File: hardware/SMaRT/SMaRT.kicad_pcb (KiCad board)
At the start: 4 copper layers, 40 x 105 mm, 29 parts, among them J1 Glider, J10 Conn_01x08, J11 Conn_01x08, J13 Power_TP, J2 Sensor, J3 TestPins_Sensor, J4 TestPins_Sensor, J5 Programmer, J6 Conn_01x03, J6 Conn_02x04_Odd_Even, J7 Conn_01x04, J8 Conn_01x04, J9 Conn_01x06, U1 MP1584, U2 MAX3232_SPARKFUN, U3 MAX3232_SPARKFUN

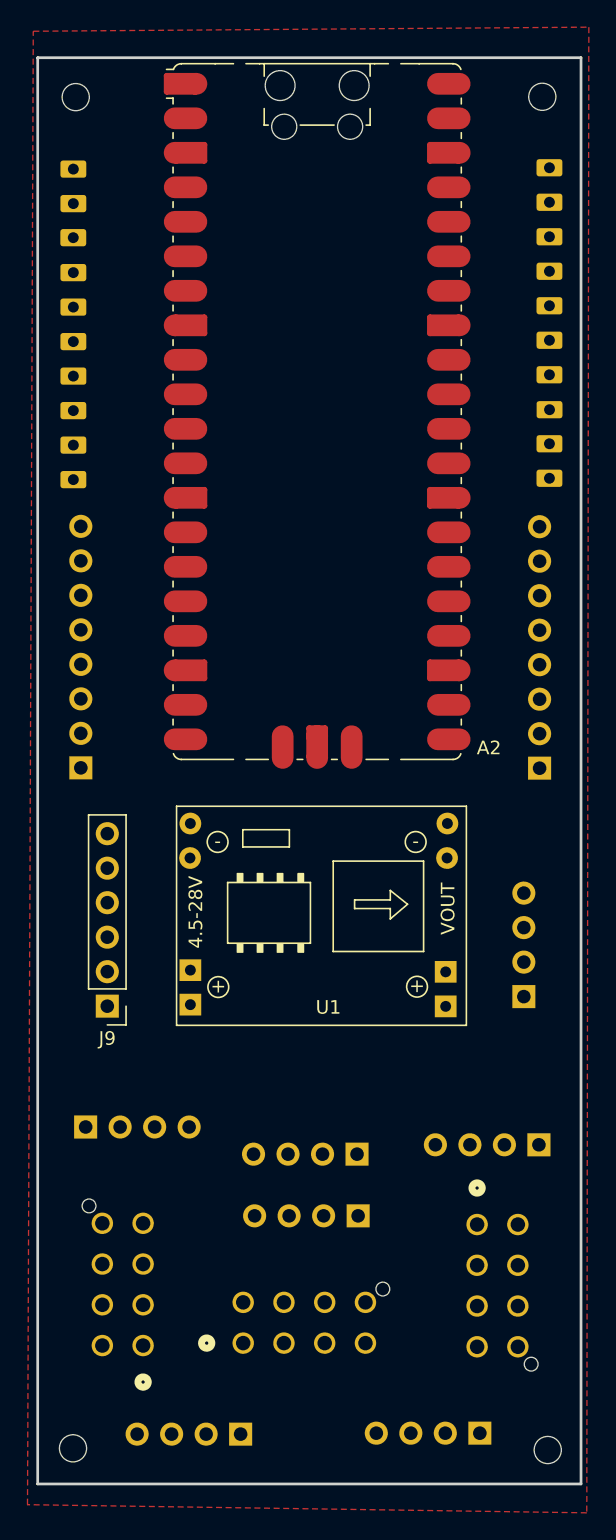
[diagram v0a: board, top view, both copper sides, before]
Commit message: added openlog, relay, switch
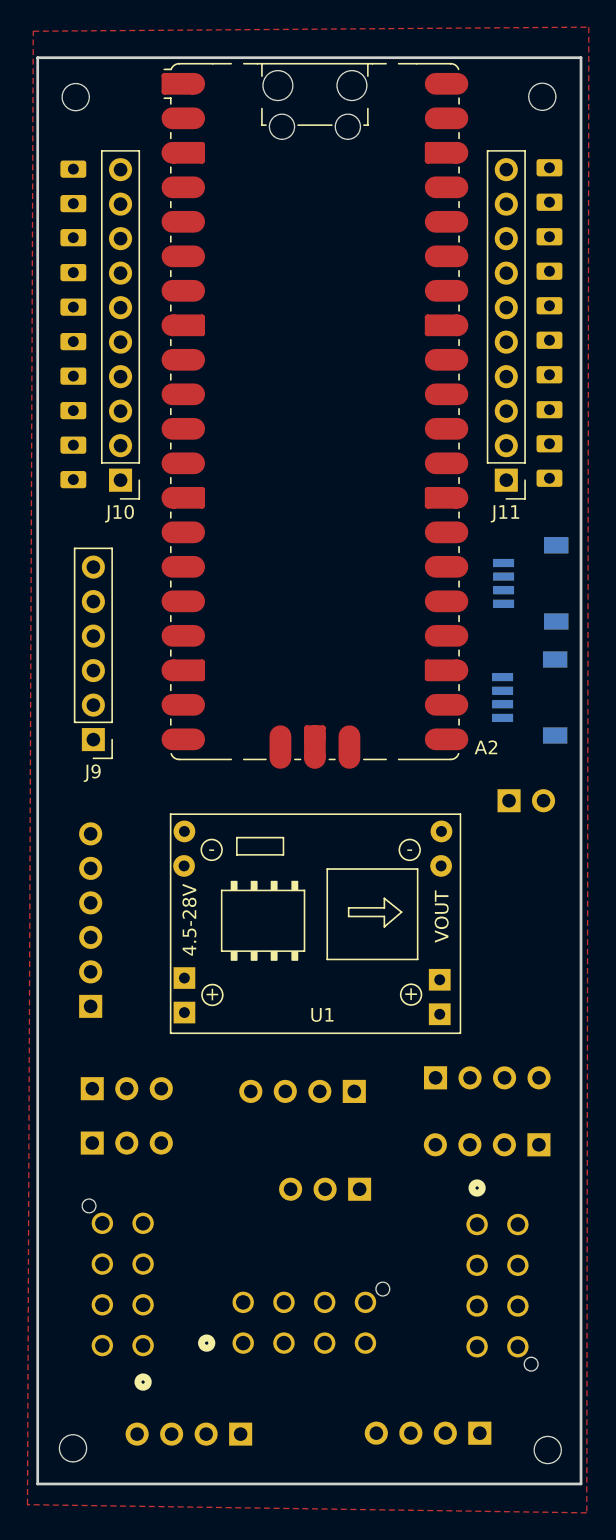
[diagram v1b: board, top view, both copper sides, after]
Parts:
- removed the J6 at (91.4, 117.1)
- added J12: Qwiic_Connector, Qwiic:Qwiic, B.Cu at (104.6, 75.1)
- added J13: Qwiic_Connector, Qwiic:Qwiic, B.Cu at (104.5, 83.5)
- added J14: SWITCH, Connector_PinHeader_2.54mm:PinHeader_1x02_P2.54mm_Vertical, B.Cu at (102.6, 91.1)
- added JP1: Jumper_3_Open, Connector_PinHeader_2.54mm:PinHeader_1x03_P2.54mm_Vertical, B.Cu at (71.9, 112.3)
- added JP2: Jumper_3_Open, Connector_PinHeader_2.54mm:PinHeader_1x03_P2.54mm_Vertical, B.Cu at (71.9, 116.3)
- added U4: OPENLOG, OpenLog:OpenLog, B.Cu at (70.4, 108.0)
- J10, J11: value Conn_01x08 -> Conn_01x10; footprint Connector_PinHeader_2.54mm:PinHeader_1x08_P2.54mm_Vertical -> Connector_PinHeader_2.54mm:PinHeader_1x10_P2.54mm_Vertical; moved to F.Cu
- J3: value TestPins_Sensor -> TestPins_Glider
- J6: footprint Connector_PinHeader_2.54mm:PinHeader_1x04_P2.54mm_Vertical -> Connector_PinHeader_2.54mm:PinHeader_1x03_P2.54mm_Vertical
- U1: footprint MPT1584:SRT_MPT1584EN_Module -> MPT1684:MPT1584EN_Module
- moved J13 26.0 mm to (97.2, 111.5)
- moved J10 21.4 mm to (74.0, 67.5), turned to 180 degrees
- moved J11 21.3 mm to (102.4, 67.5), turned to 180 degrees
- moved J9 19.7 mm to (72.0, 86.6)
- moved J4 14.3 mm to (91.2, 112.5), turned to 90 degrees
- moved J6 1.96 mm to (91.6, 119.7)
- moved U1 0.73 mm to (88.8, 99.6)
- moved A2 0.17 mm to (88.3, 62.5)
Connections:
- A2 pad 16: unconnected-(A2-GPIO12-Pad16) -> Net-(A2-GPIO12)
- A2 pad 17: unconnected-(A2-GPIO13-Pad17) -> Net-(A2-GPIO13)
- A2 pad 19: unconnected-(A2-GPIO14-Pad19) -> Net-(A2-GPIO14)
- A2 pad 20: unconnected-(A2-GPIO15-Pad20) -> Net-(A2-GPIO15)
- A2 pad 21: unconnected-(A2-GPIO16-Pad21) -> Net-(A2-GPIO16)
- A2 pad 22: unconnected-(A2-GPIO17-Pad22) -> Net-(A2-GPIO17)
- A2 pad 4: Net-(A2-GPIO2) -> /SDA1
- A2 pad 5: Net-(A2-GPIO3) -> /SCL1
- J1 pad 3: Net-(U2-T1OUT) -> /G_RX
- J10 pad 1: Net-(A2-GPIO11) -> Net-(A2-GPIO15)
- J10 pad 2: Net-(A2-GPIO10) -> Net-(A2-GPIO14)
- J10 pad 3: Net-(A2-GPIO9) -> Net-(A2-GPIO13)
- J10 pad 4: Net-(A2-GPIO8) -> Net-(A2-GPIO12)
- J10 pad 5: Net-(A2-GPIO7) -> Net-(A2-GPIO11)
- J10 pad 6: Net-(A2-GPIO6) -> Net-(A2-GPIO10)
- J10 pad 7: Net-(A2-GPIO3) -> Net-(A2-GPIO9)
- J10 pad 8: Net-(A2-GPIO2) -> Net-(A2-GPIO8)
- J11 pad 1: Net-(A2-GPIO18) -> Net-(A2-GPIO16)
- J11 pad 2: Net-(A2-GPIO19) -> Net-(A2-GPIO17)
- J11 pad 3: Net-(A2-GPIO20) -> Net-(A2-GPIO18)
- J11 pad 4: Net-(A2-GPIO21) -> Net-(A2-GPIO19)
- J11 pad 5: Net-(A2-ADC_VREF) -> Net-(A2-GPIO20)
- J11 pad 6: Net-(A2-GPIO26_ADC0) -> Net-(A2-GPIO21)
- J11 pad 7: Net-(A2-GPIO27_ADC1) -> Net-(A2-ADC_VREF)
- J11 pad 8: Net-(A2-AGND) -> Net-(A2-GPIO26_ADC0)
- J2 pad 3: /S_TX -> /S_RX
- J2 pad 4: /S_RX -> /S_TX
- J3 pad 3: VCC -> /G_RX
- U1 pad 1: VCC -> Net-(J14-Pin_1)
- U1 pad 2: VCC -> Net-(J14-Pin_1)
- U2 pad 1: Net-(U2-T1OUT) -> /G_RX
- U3 pad 10: /RX1 -> /S_RX_TTL
- U3 pad 8: /TX1 -> /S_TX_TTL
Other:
- board text added: "3V3"
- board text added: "5"
- board text added: "5V"
- board text added: "6"
- board text added: "7"
- board text added: "8"
- board text added: "OL"
- board text added: "RP"
- board text added: "SWITCH"

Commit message: relay addition
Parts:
- added JP3: Jumper_3_Open, Connector_PinHeader_2.54mm:PinHeader_1x03_P2.54mm_Vertical, B.Cu at (90.0, 117.5)
- added R1: R, Resistor_THT:R_Axial_DIN0207_L6.3mm_D2.5mm_P7.62mm_Horizontal, F.Cu at (75.0, 103.7)
- added U5: ~, G3VM-41AY1:G3VM-41AY1, F.Cu at (103.7, 100.9)
- J14: value SWITCH -> Conn_01x02
- moved J6 2.26 mm to (90.0, 121.3)
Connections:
- A2 pad 21: Net-(A2-GPIO16) -> /RELAY
- A2 pad 29: unconnected-(A2-GPIO22-Pad29) -> Net-(A2-GPIO22)
- J11 pad 1: Net-(A2-GPIO16) -> Net-(A2-GPIO17)
- J11 pad 2: Net-(A2-GPIO17) -> Net-(A2-GPIO18)
- J11 pad 3: Net-(A2-GPIO18) -> Net-(A2-GPIO19)
- J11 pad 4: Net-(A2-GPIO19) -> Net-(A2-GPIO20)
- J11 pad 5: Net-(A2-GPIO20) -> Net-(A2-GPIO21)
- J11 pad 6: Net-(A2-GPIO21) -> Net-(A2-GPIO22)
- J2 pad 1: GND -> Net-(JP3-C)
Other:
- board text added: "RLY"

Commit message: hardware: update SMaRT board and ignore KiCad artifacts
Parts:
- removed the J13 at (97.2, 111.5)
- removed REF** (x4): MountingHole_2mm, MountingHole:MountingHole_2mm
- J13: renamed from J2; footprint Library:CONN_2068320000-SD_08_MOL -> MolexLib:CONN_2068320000-SD_08_MOL
- J5: renamed from J1; footprint Library:CONN_2068320000-SD_08_MOL -> MolexLib:CONN_2068320000-SD_08_MOL
- J8: renamed from J5; footprint Library:CONN_2068320000-SD_08_MOL -> MolexLib:CONN_2068320000-SD_08_MOL
- renumbered A2 to A1, J3 to J1, J9 to J10, J4 to J12, J7 to J14, J13 to J2, J12 to J3, J14 to J4, J8 to J6, J10 to J7, J6 to J9, JP3 to JP1, JP1 to JP2, JP2 to JP3, U5 to U3, U3 to U4, U4 to U5
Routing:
- removed copper zone on F.Cu, net GND

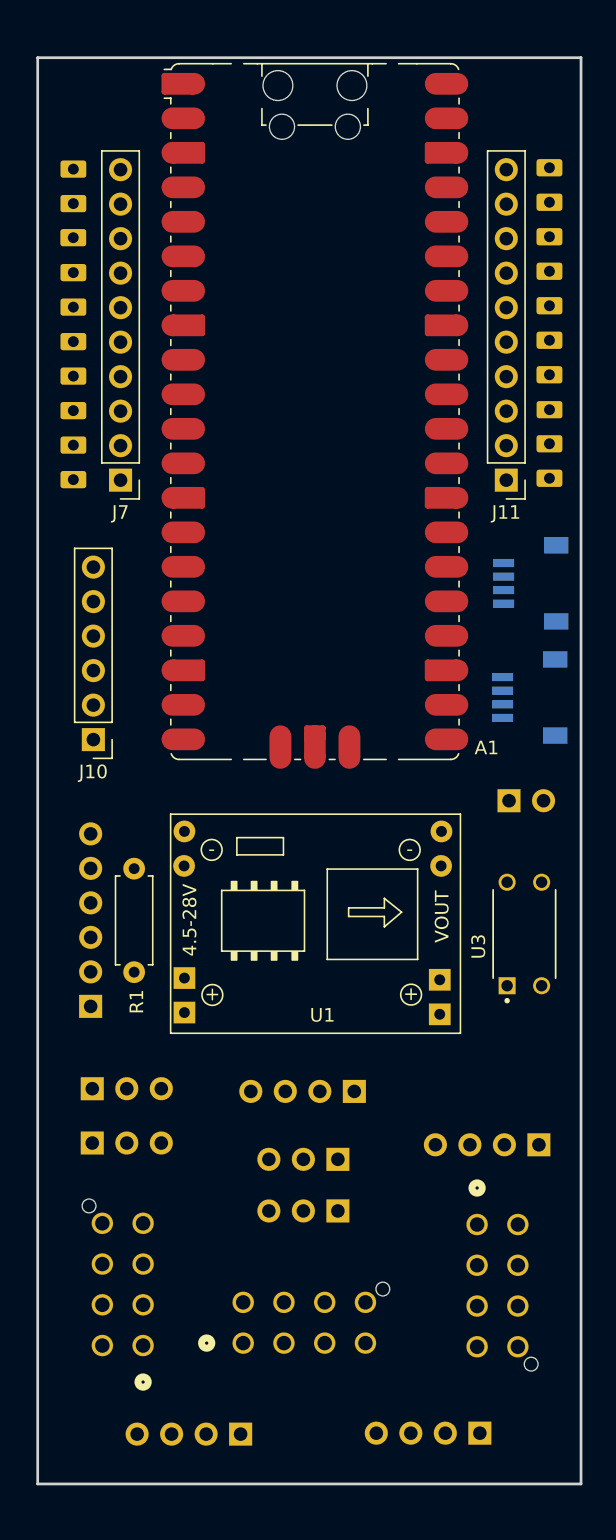
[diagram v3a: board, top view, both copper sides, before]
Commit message: hardware: add mounting holes and power test header
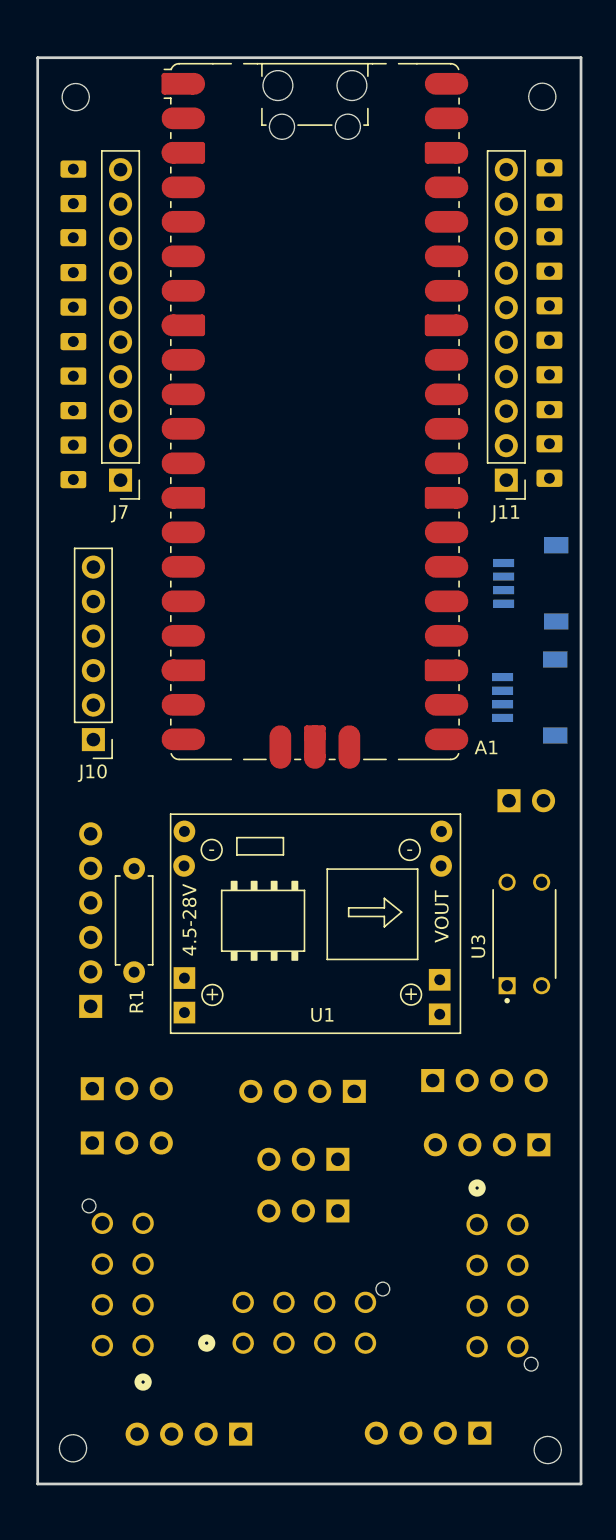
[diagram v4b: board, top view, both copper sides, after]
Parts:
- added J13: Power_TP, Connector_PinHeader_2.54mm:PinHeader_1x04_P2.54mm_Vertical, B.Cu at (97.0, 111.7)
- added REF**: MountingHole_2mm, MountingHole:MountingHole_2mm, F.Cu at (105.4, 138.9)
- added REF**: MountingHole_2mm, MountingHole:MountingHole_2mm, F.Cu at (70.7, 39.3)
- added REF**: MountingHole_2mm, MountingHole:MountingHole_2mm, F.Cu at (70.5, 138.8)
- added REF**: MountingHole_2mm, MountingHole:MountingHole_2mm, F.Cu at (105.0, 39.3)

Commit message: hardware: update PCB and schematic
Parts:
- removed the J13 at (97.0, 111.7)
- J10: value Conn_01x06 -> Power_TP; moved to B.Cu
- turned J10 to 0 degrees
- renumbered G*** to G1, G*** to G2, G*** to G3, G*** to G4, G*** to G5, G*** to G6, G*** to G7, G*** to G8, REF** to H1, REF** to H2, REF** to H3, REF** to H4
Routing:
- net GND: track 0.00 -> 290.7 mm, vias 0 -> 4
- net /3V3: track 0.00 -> 130.7 mm, vias 0 -> 3
- net VCC: track 0.00 -> 125.7 mm, vias 0 -> 1
- net +5V: track 0.00 -> 124.1 mm, vias 0 -> 1
- net /S_RX: track 0.00 -> 98.5 mm
- net /G_TX: track 0.00 -> 95.8 mm, vias 0 -> 1
- net /G_RX: track 0.00 -> 94.7 mm, vias 0 -> 1
- net /S_TX: track 0.00 -> 88.1 mm
- net /RESET: track 0.00 -> 70.6 mm, vias 0 -> 1
- net /RX1: track 0.00 -> 64.9 mm, vias 0 -> 1
- net /S_TX_TTL: track 0.00 -> 62.9 mm
- net /TX1: track 0.00 -> 62.0 mm, vias 0 -> 1
- net /S_RX_TTL: track 0.00 -> 61.8 mm
- net /SDA1: track 0.00 -> 53.2 mm, vias 0 -> 1
- net /SCL1: track 0.00 -> 48.1 mm, vias 0 -> 1
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
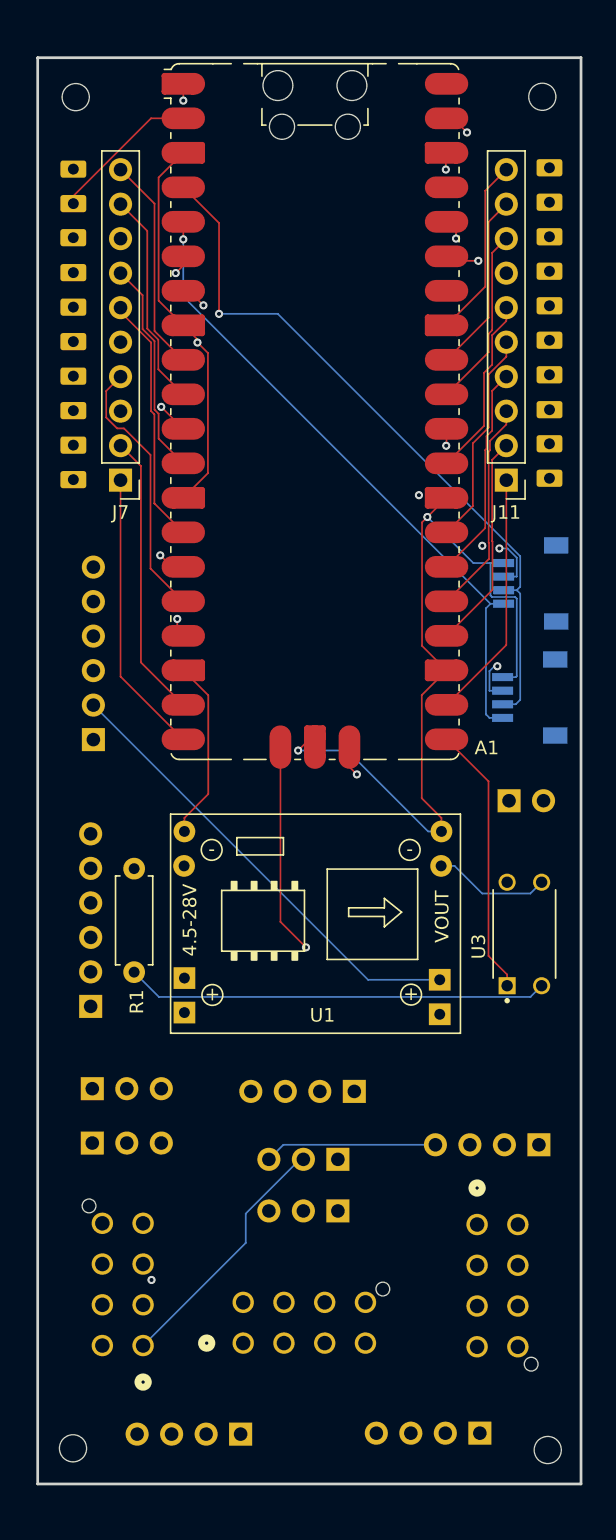
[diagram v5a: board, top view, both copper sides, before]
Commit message: First version of the SMaRT cabling
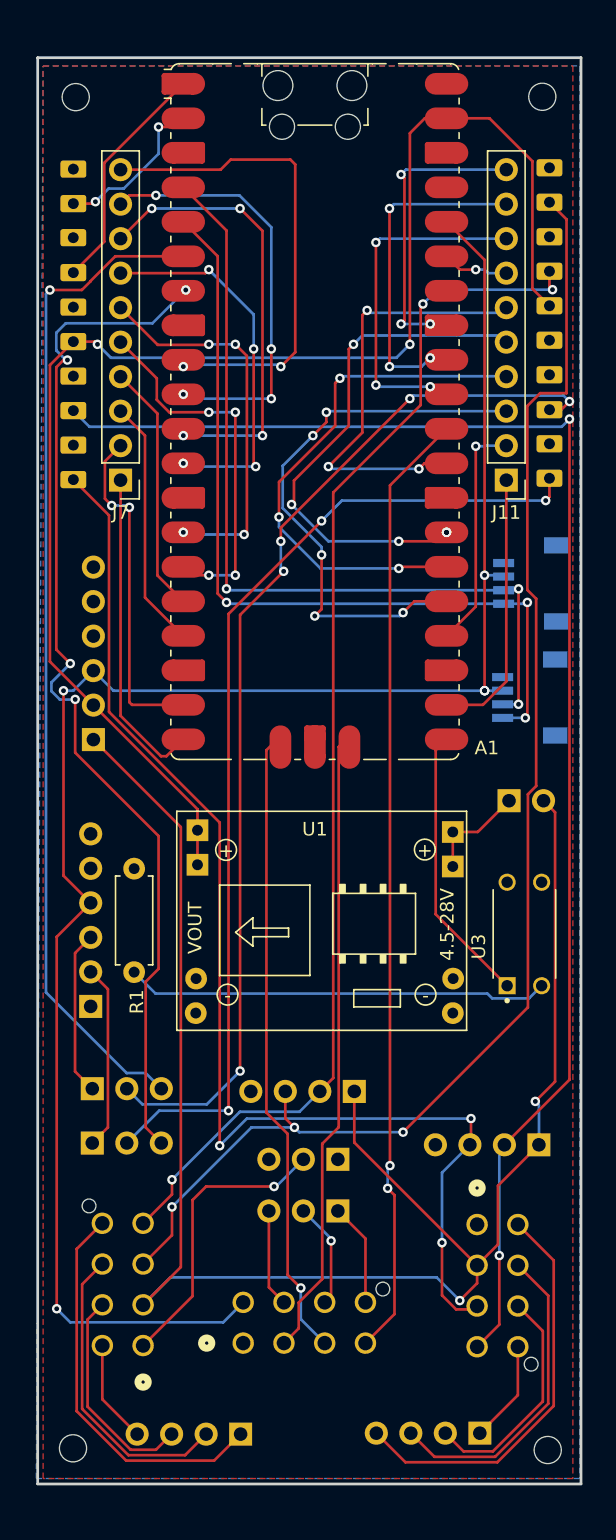
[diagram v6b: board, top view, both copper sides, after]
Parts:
- moved U1 1.09 mm to (88.3, 100.5), turned to 180 degrees
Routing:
- net GND: track 290.7 -> 0.37 mm, vias 4 -> 0
- net Net-(JP1-A): track 25.6 -> 0.00 mm
- net Net-(A1-GPIO19): track 15.8 -> 41.2 mm, vias 0 -> 5
- net Net-(J4-Pin_1): track 31.8 -> 7.63 mm
- net Net-(A1-GPIO20): track 15.8 -> 38.8 mm, vias 0 -> 3
- net Net-(A1-GPIO21): track 15.8 -> 38.6 mm, vias 0 -> 5
- net Net-(A1-GPIO6): track 15.9 -> 35.9 mm, vias 0 -> 2
- net Net-(A1-GPIO22): track 13.3 -> 32.1 mm, vias 0 -> 3
- net +5V: track 124.1 -> 106.9 mm, vias 1 -> 2
- net Net-(A1-GPIO8): track 15.9 -> 33.0 mm, vias 1 -> 4
- net Net-(A1-GPIO7): track 15.9 -> 31.6 mm, vias 0 -> 4
- net /S_TX_TTL: track 62.9 -> 78.4 mm, vias 0 -> 5
- net /SCL1: track 48.1 -> 61.8 mm, vias 1 -> 3
- net /G_TX: track 95.8 -> 108.4 mm, vias 1 -> 2
- net /RX1: track 64.9 -> 77.4 mm, vias 1 -> 4
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- added copper zone on B.Cu, net GND
- added copper zone on F.Cu, net GND
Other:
- copper layers 4 -> 2

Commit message: Modifications of the GND connexions
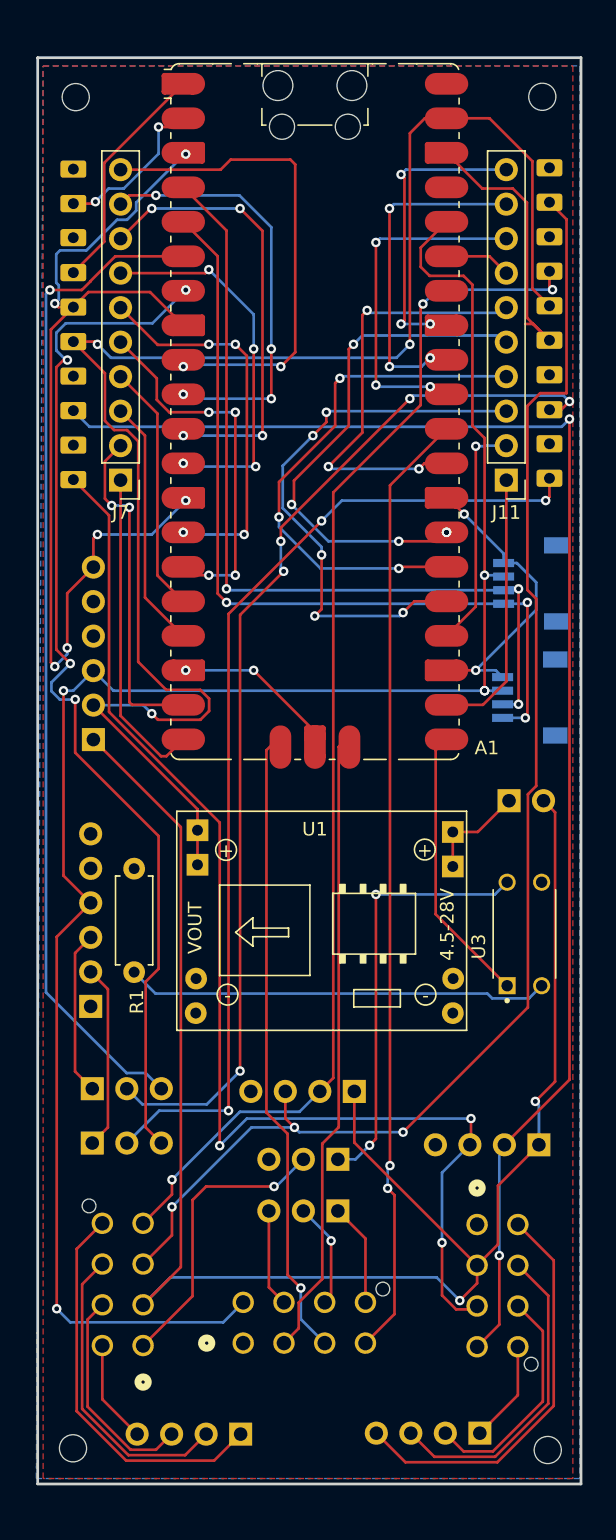
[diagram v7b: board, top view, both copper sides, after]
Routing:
- net GND: track 0.37 -> 129.0 mm, vias 0 -> 10
- net Net-(JP1-A): track 0.00 -> 31.5 mm, vias 0 -> 2
- net +5V: track 106.9 -> 120.7 mm, vias 2 -> 3
- net /3V3: track 132.8 -> 135.8 mm
- net Net-(A1-ADC_VREF): vias 1 -> 0
